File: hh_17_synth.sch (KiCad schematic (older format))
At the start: 37 parts, among them J1 USB_OTG, J3 JACK_TRS, SW1 SW_Push, SW2 SW_Push, SW3 SW_Push, U1 LM1117-3.3, U2 STM32F072CBTx, Y1 16MHz

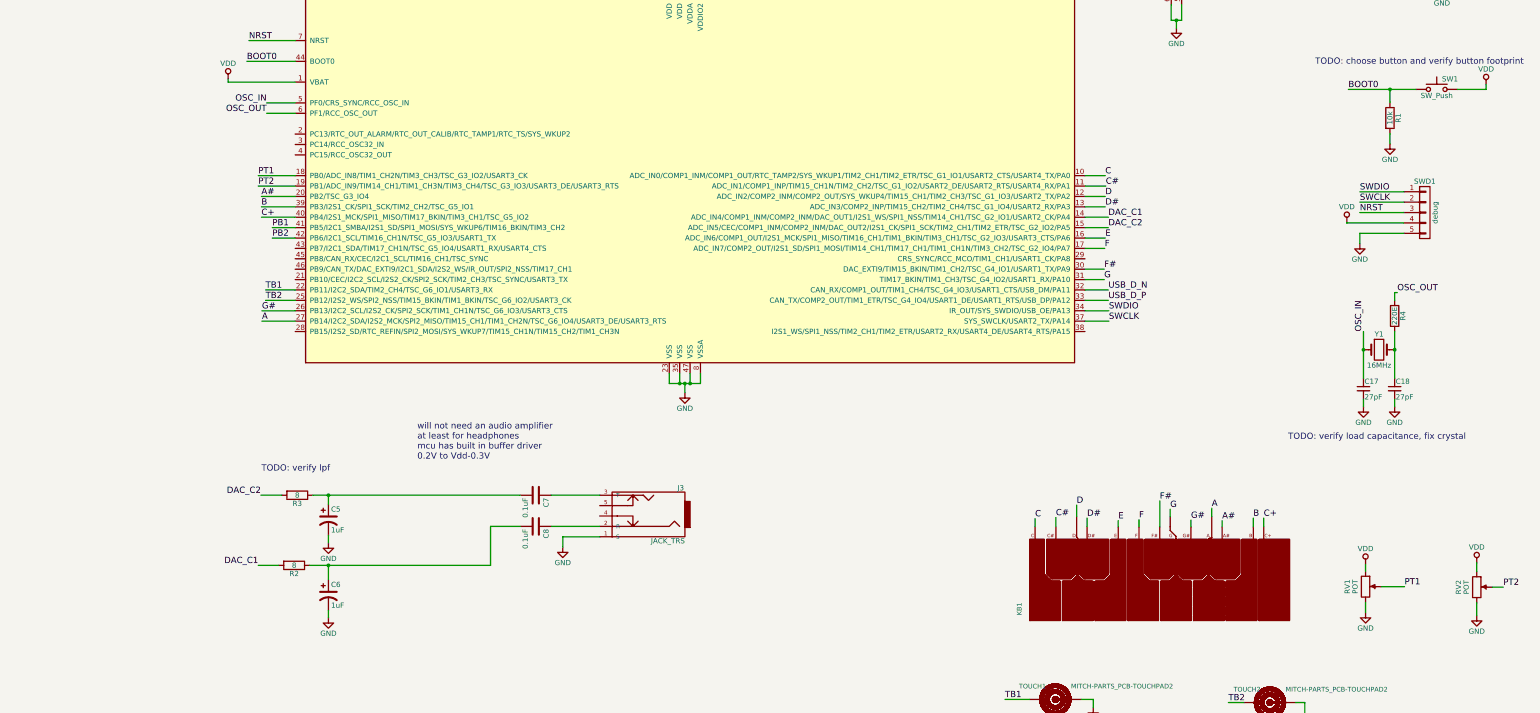
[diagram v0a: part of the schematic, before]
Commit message: added audio amp, uart port, leds
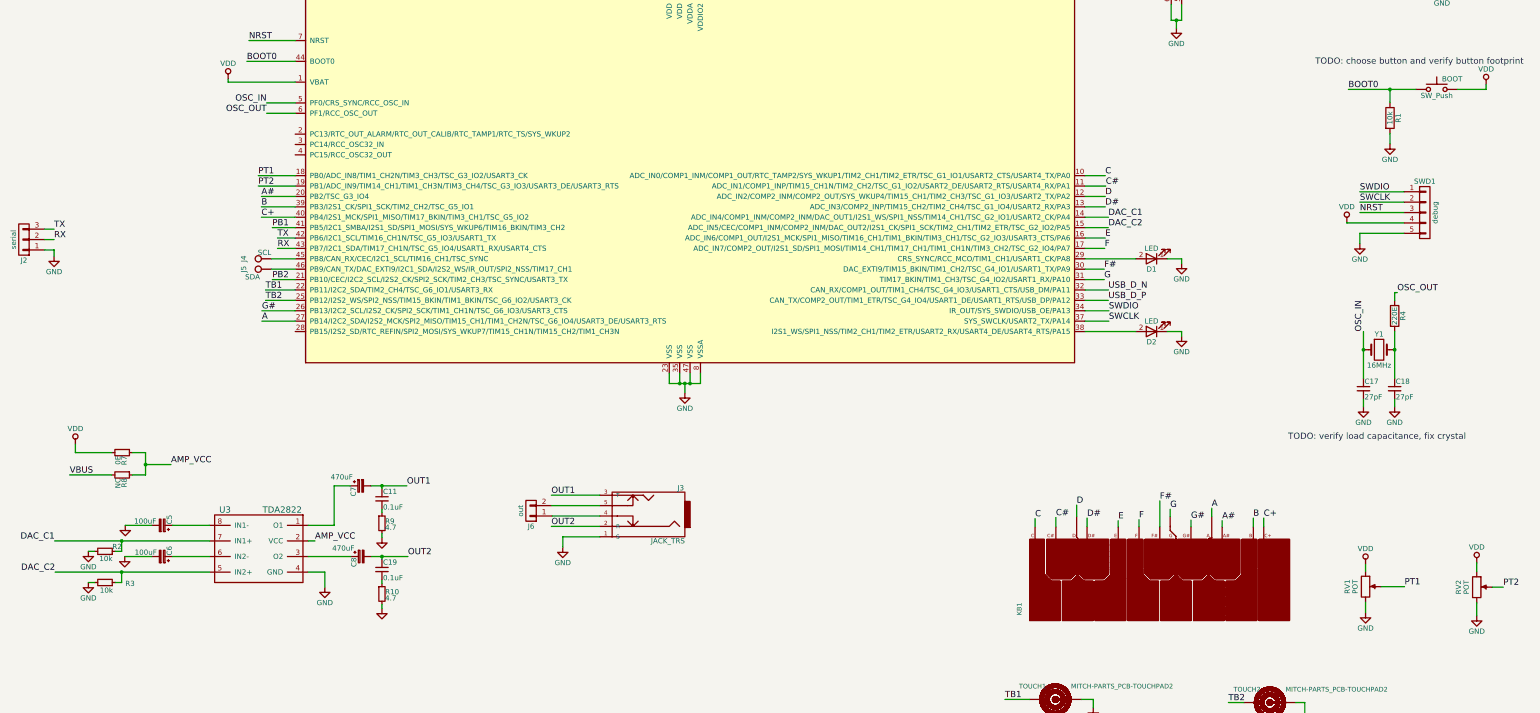
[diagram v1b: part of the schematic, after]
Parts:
- removed C5, C6: 1uF, Capacitors_THT:CP_Radial_D5.0mm_P2.00mm, symbol CP1
- removed C7, C8: 0.1uF, Capacitors_SMD:C_0603, symbol C
- removed R2, R3: 8, Resistors_SMD:R_0603, symbol R
- added C11, C19: 0.1uF, Capacitors_SMD:C_0603, symbol C_Small
- added C5, C6: 100uF, Capacitors_THT:CP_Radial_D6.3mm_P2.50mm, symbol CP_Small
- added C7, C8: 470uF, Capacitors_THT:CP_Radial_D6.3mm_P2.50mm, symbol CP_Small
- added D1, D2: LED, LEDs:LED_0603, symbol LED
- added J2: serial, Pin_Headers:Pin_Header_Straight_1x03_Pitch2.54mm, symbol CONN_01X03
- added J4: SCL, Measurement_Points:Measurement_Point_Round-TH_Small, symbol TEST_1P
- added J5: SDA, Measurement_Points:Measurement_Point_Round-TH_Small, symbol TEST_1P
- added J6: out, Pin_Headers:Pin_Header_Straight_1x02_Pitch2.54mm, symbol CONN_01X02
- added R10, R9: 4.7, Resistors_SMD:R_0603, symbol R_Small
- added R2, R3: 10k, Resistors_SMD:R_0603, symbol R_Small
- added R7: 0E, Resistors_SMD:R_0603, symbol R_Small
- added R8: NC, Resistors_SMD:R_0603, symbol R_Small
- added U3: TDA2822, Housings_SOIC:SOIC-8_3.9x4.9mm_Pitch1.27mm, symbol TDA2822
- renumbered SW1 to BOOT
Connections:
- net DAC_C1: now also R2.1, U3.7 (IN1+)
- net DAC_C2: now also R3.1, U3.5 (IN2+)
- net GND: now also C5.2, C6.2, D1.1 (K), D2.1 (K), J2.1 (P1), R10.2, R2.2, R3.2, R9.2, U3.4 (GND)
- net PB2: now also U2.21 (PB10/CEC/I2C2_SCL/I2S2_CK/SPI2_SCK/TIM2_CH3/TSC_SYNC/USART3_TX); no longer U2.42 (PB6/I2C1_SCL/TIM16_CH1N/TSC_G5_IO3/USART1_TX)
- net VBUS: now also R8.2
- net VDD: now also R7.2
- net OUT2: now reaches J3.2 (R)
- net OUT2: now also C19.1, C8.2
- net OUT1: now reaches J3.3 (T)
- net OUT1: now also C11.1, C7.2
- net at J3.4: now also J6.1 (P1)
- net at J3.5: now also J6.2 (P2)
- net at U2.29 (CRS_SYNC/RCC_MCO/TIM1_CH1/USART1_CK/PA8): now also D1.2 (A)
- net at U2.38 (I2S1_WS/SPI1_NSS/TIM2_CH1/TIM2_ETR/USART2_RX/USART4_DE/USART4_RTS/PA15): now also D2.2 (A)
- net RX: now reaches U2.43 (PB7/I2C1_SDA/TIM17_CH1N/TSC_G5_IO4/USART1_RX/USART4_CTS)
- net RX: now also J2.2 (P2)
- net at U2.45 (PB8/CAN_RX/CEC/I2C1_SCL/TIM16_CH1/TSC_SYNC): now also J4.1
- net at U2.46 (PB9/CAN_TX/DAC_EXTI9/I2C1_SDA/I2S2_WS/IR_OUT/SPI2_NSS/TIM17_CH1): now also J5.1
- new net: C7.1, U3.1 (O1)
- new net: C8.1, U3.3 (O2)
- new net: C6.1, U3.6 (IN2-)
- new net: C5.1, U3.8 (IN1-)
- new net: C11.2, R9.1
- new net: C19.2, R10.1
- new net AMP_VCC: R7.1, R8.1, U3.2 (VCC)
- new net TX: J2.3 (P3), U2.42 (PB6/I2C1_SCL/TIM16_CH1N/TSC_G5_IO3/USART1_TX)
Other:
- note removed: "TODO: verify lpf"
- note removed: "will not need an audio amplifier\nat least for headphones\nmcu has built in buffer driver\n0.2V to Vdd-0.3V"

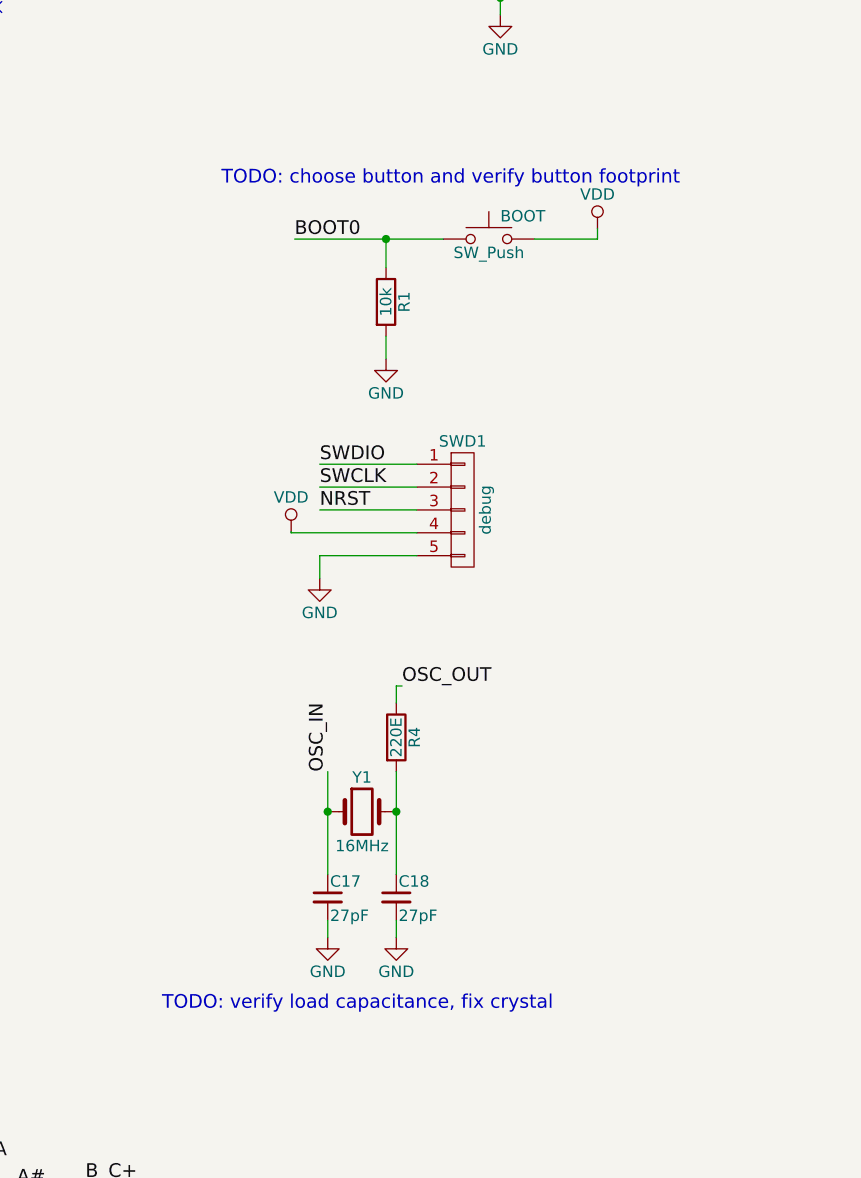
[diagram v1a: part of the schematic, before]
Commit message: smaller caps remove in-schematic comments updated preview image
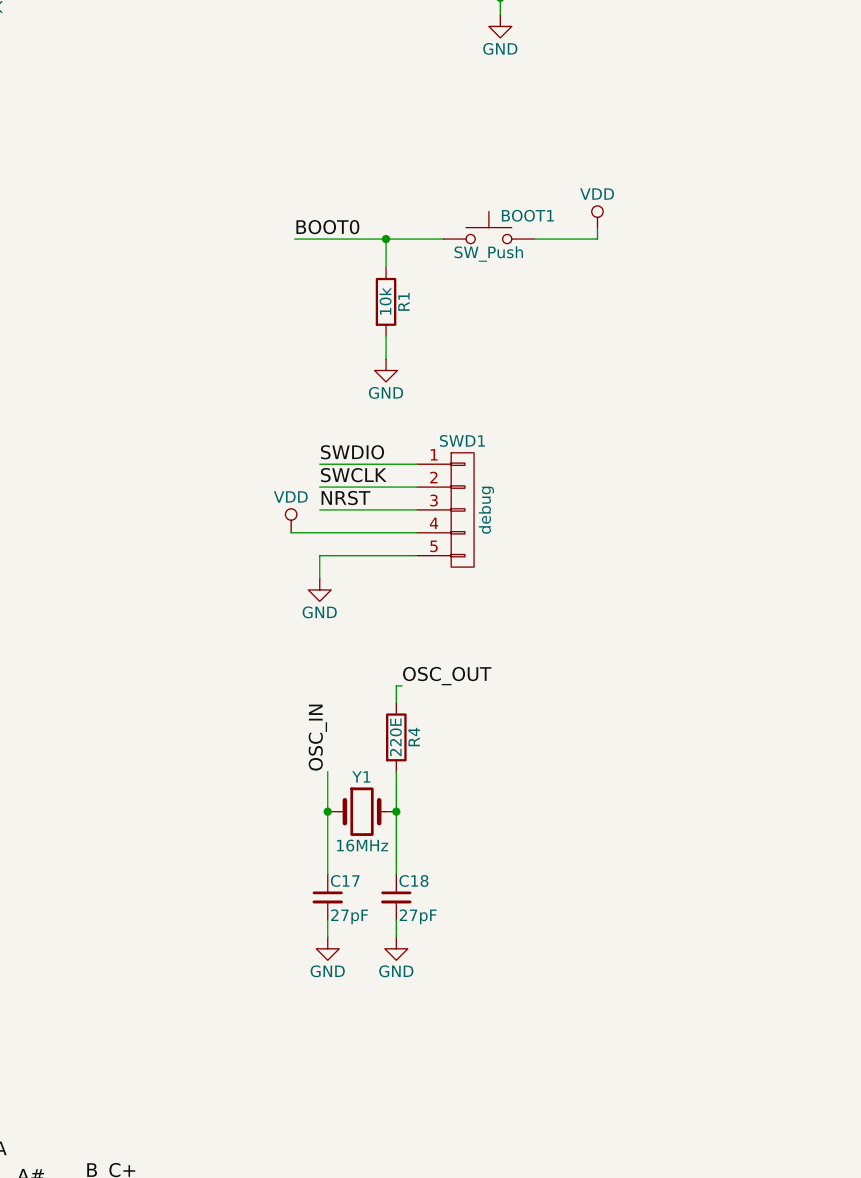
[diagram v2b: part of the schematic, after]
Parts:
- C5, C6, C7, C8: footprint Capacitors_THT:CP_Radial_D6.3mm_P2.50mm -> Capacitors_THT:CP_Radial_D5.0mm_P2.00mm
- J4, J5: footprint Measurement_Points:Measurement_Point_Round-TH_Small -> Measurement_Points:Measurement_Point_Round-SMD-Pad_Small
- renumbered BOOT to BOOT1
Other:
- note removed: "TODO: choose button and verify button footprint"
- note removed: "TODO: verify load capacitance, fix crystal"
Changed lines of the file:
@@
 $EndComp
 $Comp
-L SW_Push BOOT
+L SW_Push BOOT1
 U 1 1 58A098BF
 P 14870 2955
-F 0 "BOOT" H 14920 3055 50  0000 L CNN
+F 0 "BOOT1" H 14920 3055 50  0000 L CNN
 F 1 "SW_Push" H 14870 2895 50  0000 C CNN
 F 2 "Buttons_Switches_THT:SW_PUSH_6mm" H 14870 3155 50  0001 C CNN
@@
 Text Label 12865 8855 0    60   ~ 0
 TB2
-Text Notes 13440 6335 0    60   ~ 0
-TODO: verify load capacitance, fix crystal
-Text Notes 13700 2725 0    60   ~ 0
-TODO: choose button and verify button footprint
 $Comp
 L PWR_FLAG #FLG015
@@
 F 0 "C5" H 2615 7220 50  0000 L CNN
 F 1 "100uF" V 2645 6880 50  0000 L CNN
-F 2 "Capacitors_THT:CP_Radial_D6.3mm_P2.50mm" H 2605 7150 50  0001 C CNN
+F 2 "Capacitors_THT:CP_Radial_D5.0mm_P2.00mm" H 2605 7150 50  0001 C CNN
 F 3 "" H 2605 7150 50  0001 C CNN
 	1    2605 7150
@@
 F 0 "C6" H 2615 7520 50  0000 L CNN
 F 1 "100uF" V 2645 7185 50  0000 L CNN
-F 2 "Capacitors_THT:CP_Radial_D6.3mm_P2.50mm" H 2605 7450 50  0001 C CNN
+F 2 "Capacitors_THT:CP_Radial_D5.0mm_P2.00mm" H 2605 7450 50  0001 C CNN
 F 3 "" H 2605 7450 50  0001 C CNN
 	1    2605 7450
@@
 F 0 "C7" H 4525 6840 50  0000 L CNN
 F 1 "470uF" V 4430 6845 50  0000 L CNN
-F 2 "Capacitors_THT:CP_Radial_D6.3mm_P2.50mm" H 4515 6770 50  0001 C CNN
+F 2 "Capacitors_THT:CP_Radial_D5.0mm_P2.00mm" H 4515 6770 50  0001 C CNN
 F 3 "" H 4515 6770 50  0001 C CNN
 	1    4515 6770
@@
 F 0 "C8" H 4530 7520 50  0000 L CNN
 F 1 "470uF" V 4440 7515 50  0000 L CNN
-F 2 "Capacitors_THT:CP_Radial_D6.3mm_P2.50mm" H 4520 7450 50  0001 C CNN
+F 2 "Capacitors_THT:CP_Radial_D5.0mm_P2.00mm" H 4520 7450 50  0001 C CNN
 F 3 "" H 4520 7450 50  0001 C CNN
 	1    4520 7450
@@
 F 0 "J4" H 3660 4855 50  0000 C CNN
 F 1 "SCL" V 3720 4655 50  0000 C CNN
-F 2 "Measurement_Points:Measurement_Point_Round-TH_Small" H 3860 4585 50  0001 C CNN
+F 2 "Measurement_Points:Measurement_Point_Round-SMD-Pad_Small" H 3860 4585 50  0001 C CNN
 F 3 "" H 3860 4585 50  0001 C CNN
 	1    3660 4585
@@
 F 0 "J5" H 3660 4955 50  0000 C CNN
 F 1 "SDA" V 3585 4870 50  0000 C CNN
-F 2 "Measurement_Points:Measurement_Point_Round-TH_Small" H 3860 4685 50  0001 C CNN
+F 2 "Measurement_Points:Measurement_Point_Round-SMD-Pad_Small" H 3860 4685 50  0001 C CNN
 F 3 "" H 3860 4685 50  0001 C CNN
 	1    3660 4685
